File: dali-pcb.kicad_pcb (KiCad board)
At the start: 2 copper layers, 180.3 x 113 mm, 57 parts, among them J1 12-22.5V DC, J10 LOLIN-S3 (R), J11 ESP32-S3-DEVKITC-1 (L), J12 ESP32-S3-DEVKITC-1 (R), J13 LOLIN-S2-MINI (L), J14 LOLIN-S2-MINI (R), J15 DALI BUS, J16 DALI BUS, J17 FTDI-MCU, J18 A10, J19 A5-1, J2 DALI BUS, J20 A5-2, J21 A2-1, J22 A2-2, J23 A2-3, J24 A2-4, J25 A2-5, J26 D8, J27 D4-1, J28 D4-2, J29 D2-1, J3 5V DC, J30 D2-2, J31 D2-3, J32 D2-4, J33 D1-11, J34 D1-12, J35 D1-13, J36 D1-14, J37 UART-DALI, J4 5V DC, J5 5V DC, J6 5V DC, J7 5V DC, J8 GND, J9 LOLIN-S3 (L), Q1 PZT2222A, Q2 MMBT2222A, U1 TCLT1000, U2 TCLT1000

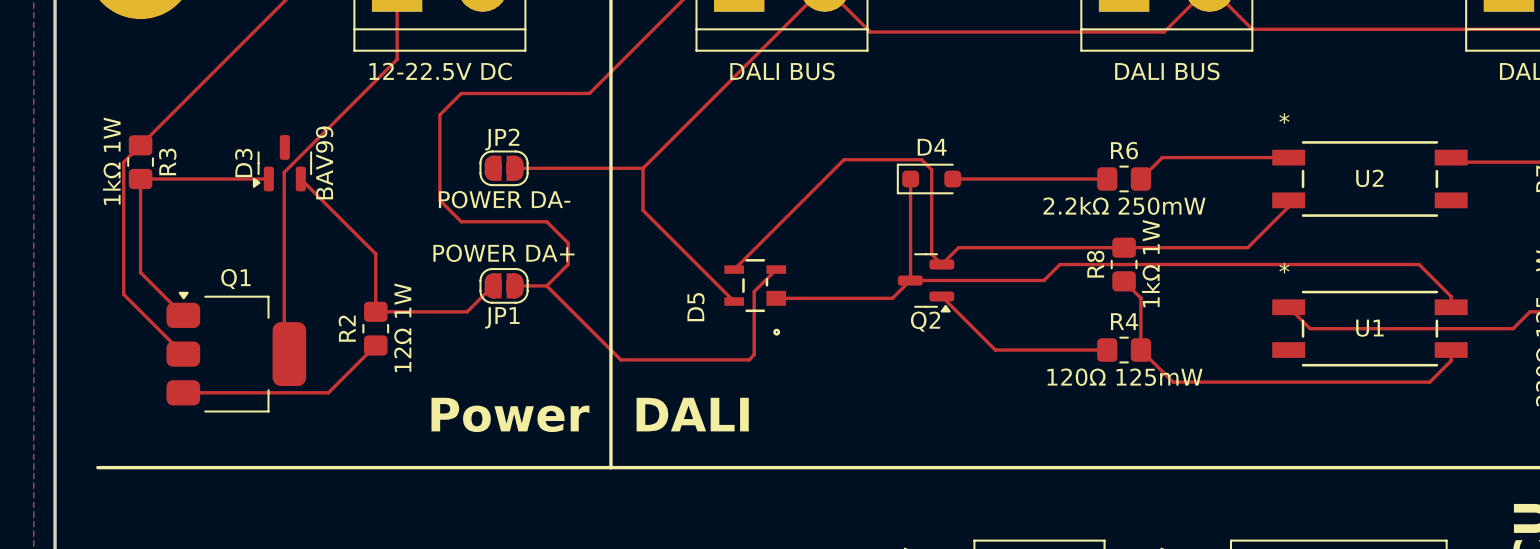
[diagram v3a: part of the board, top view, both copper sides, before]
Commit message: Rotate R3 and improve silkscreen positions
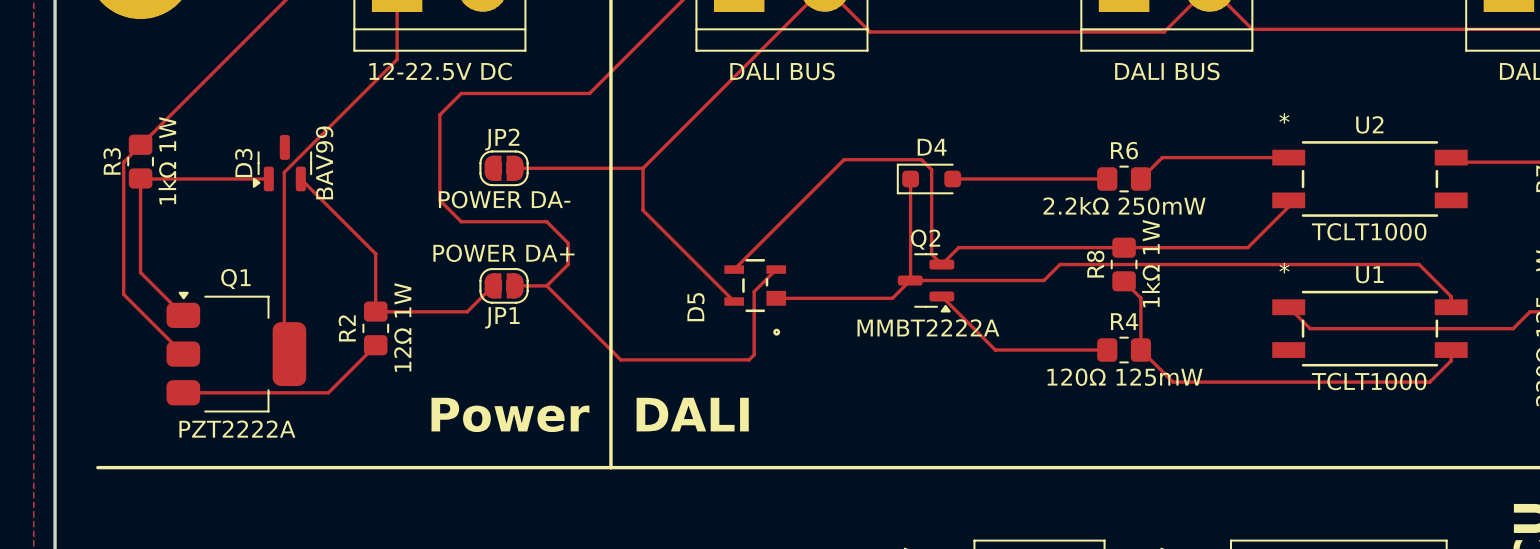
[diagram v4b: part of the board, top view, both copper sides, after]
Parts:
- turned R3 to 90 degrees
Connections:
- R3 pad 1: +12-22.5V DC -> Net-(Q1-B)
- R3 pad 2: Net-(Q1-B) -> +12-22.5V DC

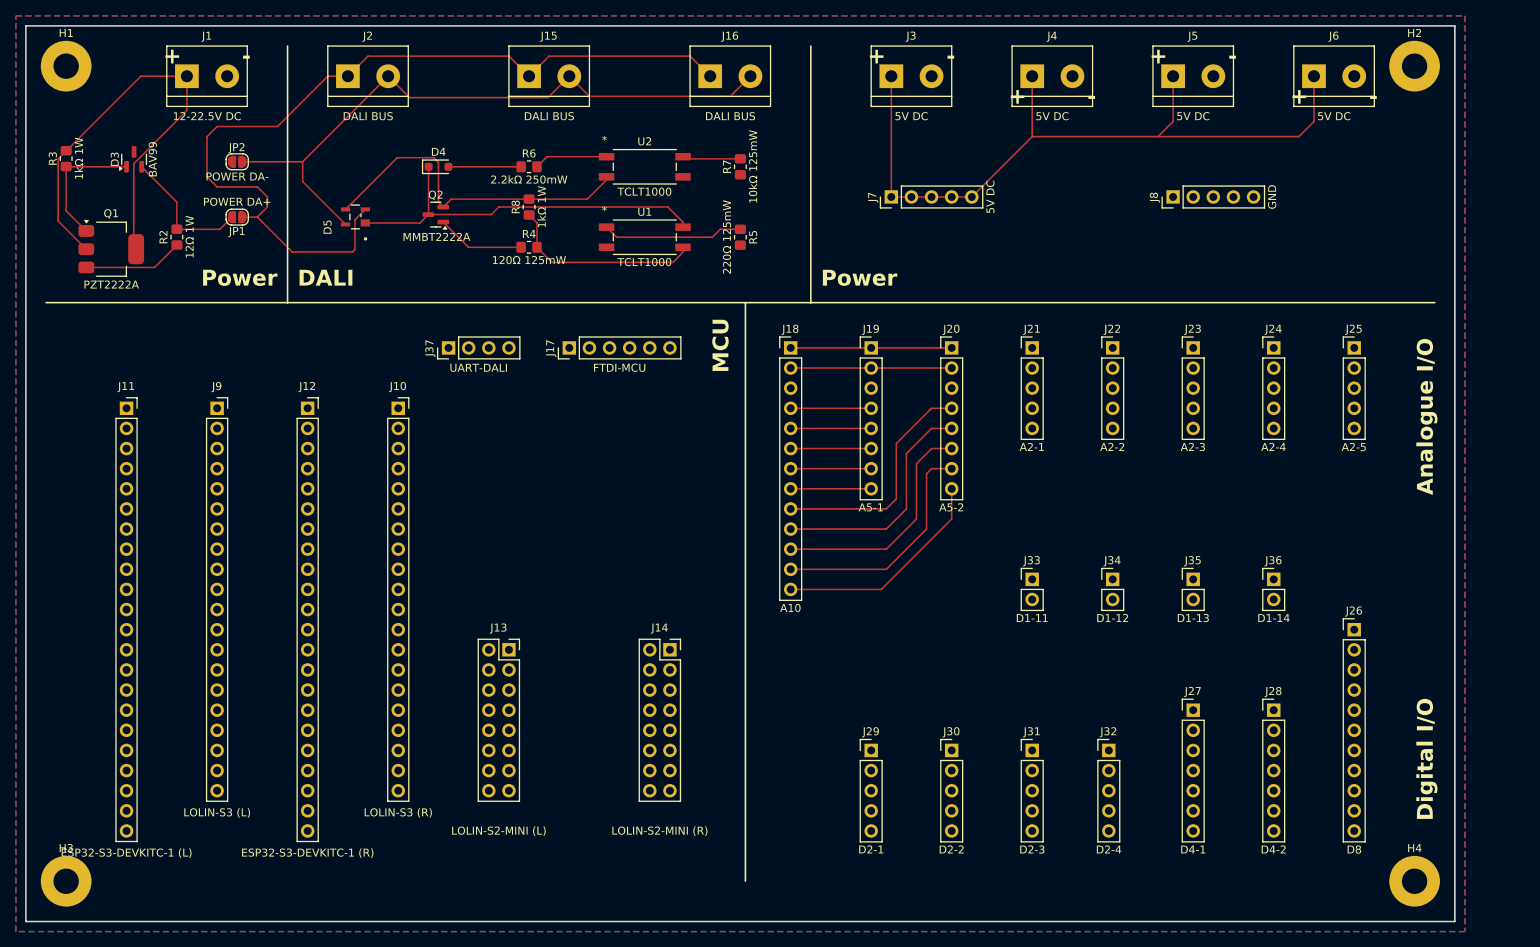
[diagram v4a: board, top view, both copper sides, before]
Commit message: Renumber references and place LOLIN-S3-MINI
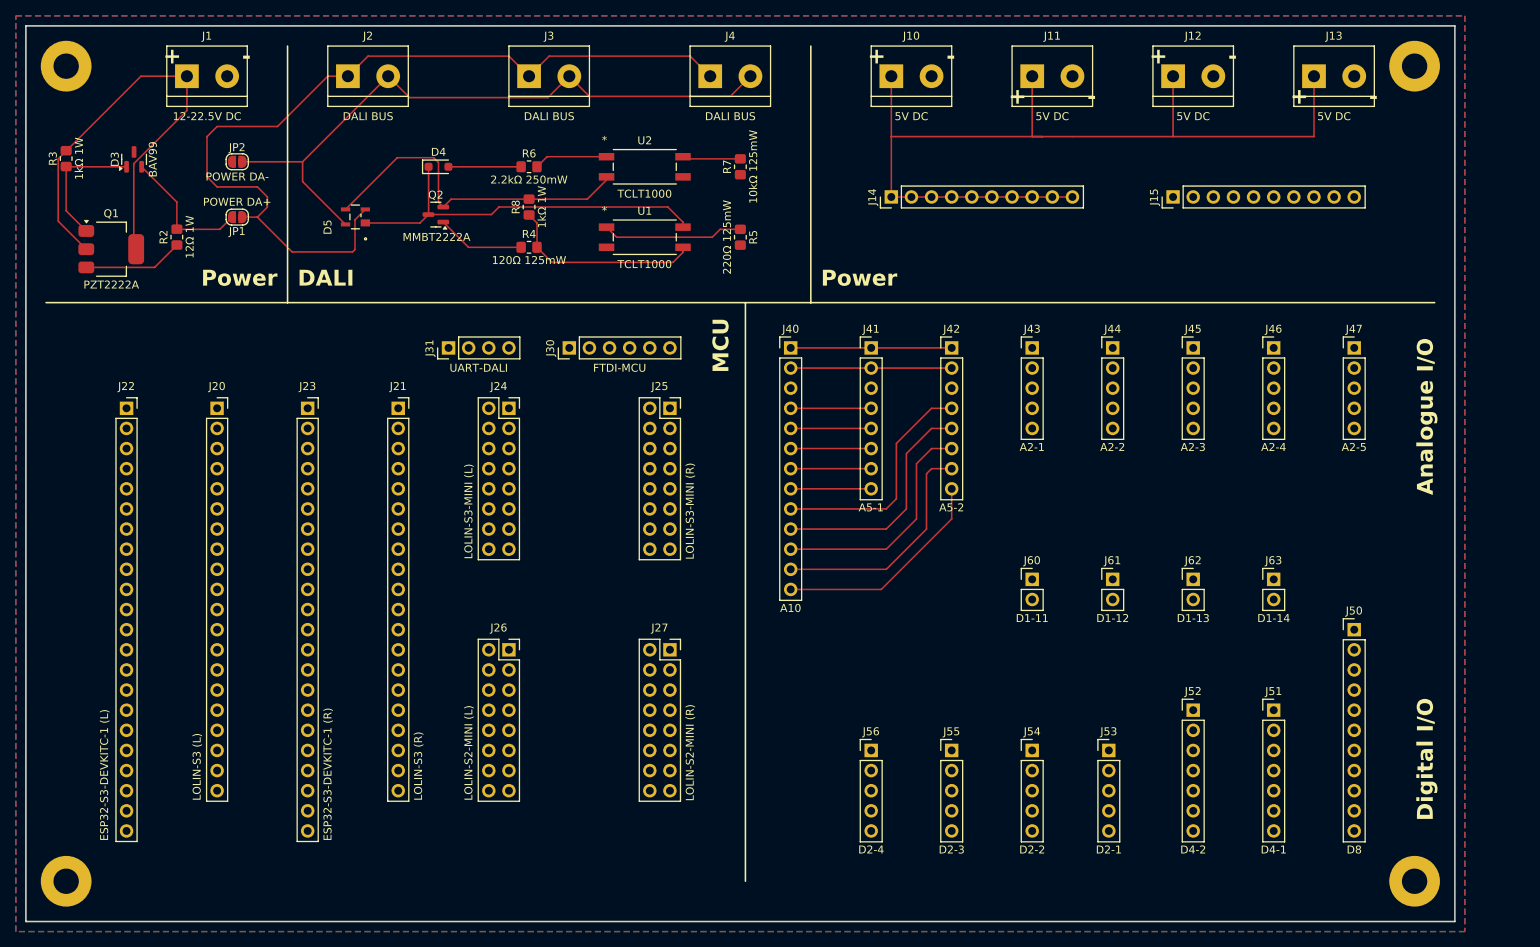
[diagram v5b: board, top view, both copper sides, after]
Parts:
- added J24: LOLIN-S3-MINI (L), Connector_PinSocket_2.54mm:PinSocket_2x08_P2.54mm_Vertical, F.Cu at (76.2, 63.5)
- added J25: LOLIN-S3-MINI (R), Connector_PinSocket_2.54mm:PinSocket_2x08_P2.54mm_Vertical, F.Cu at (96.5, 63.5)
- J14: renamed from J7; footprint Connector_PinHeader_2.54mm:PinHeader_1x05_P2.54mm_Vertical -> Connector_PinHeader_2.54mm:PinHeader_1x10_P2.54mm_Vertical
- J15: renamed from J8; footprint Connector_PinHeader_2.54mm:PinHeader_1x05_P2.54mm_Vertical -> Connector_PinHeader_2.54mm:PinHeader_1x10_P2.54mm_Vertical
- J51: renamed from J28; value D4-2 -> D4-1
- J52: renamed from J27; value D4-1 -> D4-2
- J53: renamed from J32; value D2-4 -> D2-1
- J54: renamed from J31; value D2-3 -> D2-2
- J55: renamed from J30; value D2-2 -> D2-3
- J56: renamed from J29; value D2-1 -> D2-4
- renumbered J3 to J10, J4 to J11, J5 to J12, J6 to J13, J9 to J20, J10 to J21, J11 to J22, J12 to J23, J13 to J26, J14 to J27, J15 to J3, J17 to J30, J37 to J31, J16 to J4, J18 to J40, J19 to J41, J20 to J42, J21 to J43, J22 to J44, J23 to J45, J24 to J46, J25 to J47, J26 to J50, J33 to J60, J34 to J61, J35 to J62, J36 to J63
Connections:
- J51 pad 4: /IO/IO_D16 -> /IO/IO_D11
- J51 pad 5: /IO/IO_D17 -> /IO/IO_D12
- J51 pad 6: /IO/IO_D18 -> /IO/IO_D13
- J51 pad 7: /IO/IO_D39 -> /IO/IO_D14
- J52 pad 4: /IO/IO_D11 -> /IO/IO_D16
- J52 pad 5: /IO/IO_D12 -> /IO/IO_D17
- J52 pad 6: /IO/IO_D13 -> /IO/IO_D18
- J52 pad 7: /IO/IO_D14 -> /IO/IO_D39
- J53 pad 4: /IO/IO_D18 -> /IO/IO_D11
- J53 pad 5: /IO/IO_D39 -> /IO/IO_D12
- J54 pad 4: /IO/IO_D16 -> /IO/IO_D13
- J54 pad 5: /IO/IO_D17 -> /IO/IO_D14
- J55 pad 4: /IO/IO_D13 -> /IO/IO_D16
- J55 pad 5: /IO/IO_D14 -> /IO/IO_D17
- J56 pad 4: /IO/IO_D11 -> /IO/IO_D18
- J56 pad 5: /IO/IO_D12 -> /IO/IO_D39
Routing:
- net +5V: track 114.6 -> 135.9 mm

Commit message: Add logo, URLs, version
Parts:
- added EHLAB: LOGO, LOGO, F.Cu at (112.8, 112.8)
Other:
- board text added: "V1.0.0"
- board text added: "https://edinburghhacklab.com https://github.com/edinburghhacklab/dali-pcb"
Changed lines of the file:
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@@
 		)
 	)
+	(footprint "LOGO"
+		(layer "F.Cu")
+		(at 112.776 112.776)
+		(property "Reference" "EHLAB"
+			(at 0 0 0)
+			(layer "F.SilkS")
+			(hide yes)
+			(effects
+				(font
+					(size 1.5 1.5)
+					(thickness 0.3)
+				)
+			)
+		)
+		(property "Value" "LOGO"
+			(at 0.75 0 0)
+			(layer "F.SilkS")
+			(hide yes)
+			(effects
+				(font
+					(size 1.5 1.5)
+					(thickness 0.3)
+				)
+			)
+		)
+		(property "Datasheet" ""
+			(at 0 0 0)
+			(layer "F.Fab")
+			(hide yes)
+			(effects
+				(font
+					(size 1.27 1.27)
+					(thickness 0.15)
+				)
+			)
+		)
+		(property "Description" ""
+			(at 0 0 0)
+			(layer "F.Fab")
+			(hide yes)
+			(effects
+				(font
+					(size 1.27 1.27)
+					(thickness 0.15)
+				)
+			)
+		)
+		(attr board_only exclude_from_pos_files exclude_from_bom)
+		(fp_poly
+			(pts
+				(xy 0.381 1.150055) (xy 0.381 1.919111) (xy 0 1.919111) (xy -0.381 1.919111) (xy -0.381 1.150055)
+				(xy -0.381 0.381) (xy 0 0.381) (xy 0.381 0.381)
+			)
+			(stroke
+				(width 0)
+				(type solid)
+			)
+			(fill yes)
+			(layer "F.SilkS")
+		)
+		(fp_poly
+			(pts
+				(xy 0.381 3.464278) (xy 0.381 4.233333) (xy 0 4.233333) (xy -0.381 4.233333) (xy -0.381 3.464278)
+				(xy -0.381 2.695222) (xy 0 2.695222) (xy 0.381 2.695222)
+			)
+			(stroke
+				(width 0)
+				(type solid)
+			)
+			(fill yes)
+			(layer "F.SilkS")
+		)
+		(fp_poly
+			(pts
+				(xy -1.157111 -2.30694) (xy -1.157111 -0.380547) (xy -1.541639 -0.384301) (xy -1.926167 -0.388056)
+				(xy -1.929816 -1.154132) (xy -1.933466 -1.920209) (xy -2.564816 -1.916132) (xy -2.716179 -1.915075)
+				(xy -2.841916 -1.913962) (xy -2.944623 -1.912681) (xy -3.026898 -1.91112) (xy -3.091336 -1.909169)
+				(xy -3.140535 -1.906717) (xy -3.17709 -1.90365) (xy -3.203598 -1.899859) (xy -3.222655 -1.895233)
+				(xy -3.236858 -1.889658) (xy -3.241837 -1.887097) (xy -3.324257 -1.829293) (xy -3.390494 -1.757024)
+				(xy -3.424043 -1.700492) (xy -3.456947 -1.629833) (xy -3.456947 0) (xy -3.456947 1.629833) (xy -3.424043 1.700491)
+				(xy -3.373636 1.778721) (xy -3.302067 1.847587) (xy -3.241837 1.887097) (xy -3.228865 1.893088)
+				(xy -3.212093 1.898086) (xy -3.188925 1.902203) (xy -3.156766 1.905551) (xy -3.113017 1.908239)
+				(xy -3.055084 1.910381) (xy -2.98037 1.912087) (xy -2.886278 1.913468) (xy -2.770211 1.914636) (xy -2.629574 1.915702)
+				(xy -2.564816 1.916132) (xy -1.933466 1.920208) (xy -1.929816 1.154132) (xy -1.926167 0.388055)
+				(xy -1.541639 0.384301) (xy -1.157111 0.380546) (xy -1.157111 2.30694) (xy -1.157111 4.233333) (xy -1.545167 4.233333)
+				(xy -1.933222 4.233333) (xy -1.933222 3.464278) (xy -1.933222 2.695222) (xy -2.559926 2.695222)
+				(xy -2.725689 2.695043) (xy -2.866163 2.694341) (xy -2.98428 2.692867) (xy -3.082972 2.690375) (xy -3.16517 2.686616)
+				(xy -3.233807 2.681343) (xy -3.291815 2.674307) (xy -3.342125 2.665261) (xy -3.387668 2.653957)
+				(xy -3.431378 2.640148) (xy -3.476186 2.623585) (xy -3.494919 2.616195) (xy -3.656467 2.53803) (xy -3.800366 2.438971)
+				(xy -3.89329 2.355184) (xy -4.010027 2.219179) (xy -4.104769 2.066286) (xy -4.178329 1.895187) (xy -4.179826 1.890889)
+				(xy -4.226278 1.756833) (xy -4.226278 0) (xy -4.226278 -1.756833) (xy -4.179826 -1.890889) (xy -4.106541 -2.062228)
+				(xy -4.011927 -2.2165) (xy -3.897373 -2.352217) (xy -3.76427 -2.467892) (xy -3.614007 -2.562036)
+				(xy -3.506655 -2.611436) (xy -3.458356 -2.630185) (xy -3.413091 -2.64592) (xy -3.367897 -2.658902)
+				(xy -3.319809 -2.669395) (xy -3.265862 -2.677661) (xy -3.203092 -2.683962) (xy -3.128534 -2.688561)
+				(xy -3.039224 -2.69172) (xy -2.932198 -2.693701) (xy -2.80449 -2.694766) (xy -2.653136 -2.695179)
+				(xy -2.559926 -2.695222) (xy -1.933222 -2.695222) (xy -1.933222 -3.464278) (xy -1.933222 -4.233333)
+				(xy -1.545167 -4.233333) (xy -1.157111 -4.233333)
+			)
+			(stroke
+				(width 0)
+				(type solid)
+			)
+			(fill yes)
+			(layer "F.SilkS")
+		)
+		(fp_poly
+			(pts
+				(xy 1.933222 -3.464278) (xy 1.933222 -2.695222) (xy 2.559925 -2.695222) (xy 2.723695 -2.695001)
+				(xy 2.861703 -2.694291) (xy 2.976409 -2.693027) (xy 3.07027 -2.69114) (xy 3.145744 -2.688566) (xy 3.20529 -2.685235)
+				(xy 3.251366 -2.681082) (xy 3.286429 -2.676039) (xy 3.290175 -2.67534) (xy 3.46309 -2.628274) (xy 3.623788 -2.556929)
+				(xy 3.770223 -2.463349) (xy 3.90035 -2.349581) (xy 4.012122 -2.21767) (xy 4.103494 -2.069663) (xy 4.172421 -1.907605)
+				(xy 4.213451 -1.752064) (xy 4.216789 -1.720229) (xy 4.219853 -1.662392) (xy 4.222645 -1.580772)
+				(xy 4.225163 -1.477586) (xy 4.227408 -1.355055) (xy 4.22938 -1.215396) (xy 4.231079 -1.060828) (xy 4.232505 -0.893571)
+				(xy 4.233657 -0.715842) (xy 4.234537 -0.529861) (xy 4.235143 -0.337847) (xy 4.235476 -0.142017)
+				(xy 4.235536 0.05541) (xy 4.235323 0.252214) (xy 4.234836 0.446177) (xy 4.234077 0.63508) (xy 4.233044 0.816705)
+				(xy 4.231739 0.988832) (xy 4.23016 1.149244) (xy 4.228308 1.295721) (xy 4.226182 1.426045) (xy 4.223784 1.537996)
+				(xy 4.221112 1.629357) (xy 4.218168 1.697909) (xy 4.21495 1.741432) (xy 4.213451 1.752064) (xy 4.166533 1.924258)
+				(xy 4.09533 2.084544) (xy 4.001947 2.23081) (xy 3.888493 2.360946) (xy 3.757074 2.472843) (xy 3.609798 2.56439)
+				(xy 3.448774 2.633477) (xy 3.291629 2.675132) (xy 3.257741 2.680326) (xy 3.213671 2.684616) (xy 3.156915 2.688071)
+				(xy 3.084968 2.690758) (xy 2.995326 2.692747) (xy 2.885484 2.694107) (xy 2.75294 2.694906) (xy 2.595188 2.695214)
+				(xy 2.559925 2.695222) (xy 1.933222 2.695222) (xy 1.933222 3.464278) (xy 1.933222 4.233333) (xy 1.545167 4.233333)
+				(xy 1.157111 4.233333) (xy 1.157111 2.30694) (xy 1.157111 0.380546) (xy 1.541639 0.384301) (xy 1.926167 0.388055)
+				(xy 1.929816 1.154132) (xy 1.933466 1.920208) (xy 2.564816 1.916132) (xy 2.716179 1.915075) (xy 2.841915 1.913962)
+				(xy 2.944623 1.912681) (xy 3.026898 1.91112) (xy 3.091336 1.909169) (xy 3.140534 1.906716) (xy 3.177089 1.90365)
+				(xy 3.203597 1.899859) (xy 3.222655 1.895232) (xy 3.236858 1.889658) (xy 3.241837 1.887097) (xy 3.324257 1.829292)
+				(xy 3.390494 1.757024) (xy 3.424042 1.700491) (xy 3.456946 1.629833) (xy 3.456946 0) (xy 3.456946 -1.629833)
+				(xy 3.424042 -1.700492) (xy 3.373636 -1.778721) (xy 3.302066 -1.847587) (xy 3.241837 -1.887097)
+				(xy 3.228864 -1.893088) (xy 3.212092 -1.898087) (xy 3.188925 -1.902204) (xy 3.156765 -1.905551)
+				(xy 3.113017 -1.90824) (xy 3.055084 -1.910381) (xy 2.98037 -1.912087) (xy 2.886277 -1.913468) (xy 2.770211 -1.914636)
+				(xy 2.629574 -1.915702) (xy 2.564816 -1.916132) (xy 1.933466 -1.920209) (xy 1.929816 -1.154132)
+				(xy 1.926167 -0.388056) (xy 1.541639 -0.384301) (xy 1.157111 -0.380547) (xy 1.157111 -0.768829)
+				(xy 1.157111 -1.157111) (xy 0.388055 -1.157111) (xy -0.381 -1.157111) (xy -0.381 -1.53799) (xy -0.381 -1.918868)
+				(xy 0.384528 -1.922518) (xy 1.150055 -1.926167) (xy 1.15381 -2.310695) (xy 1.157565 -2.695222) (xy 0.388282 -2.695222)
+				(xy -0.381 -2.695222) (xy -0.381 -3.083278) (xy -0.381 -3.471333) (xy 0.388055 -3.471333) (xy 1.157111 -3.471333)
+				(xy 1.157111 -3.852333) (xy 1.157111 -4.233333) (xy 1.545167 -4.233333) (xy 1.933222 -4.233333)
+			)
+			(stroke
+				(width 0)
+				(type solid)
+			)
+			(fill yes)
+			(layer "F.SilkS")
+		)
+		(embedded_fonts no)
+	)
 	(footprint "Resistor_SMD:R_0805_2012Metric_Pad1.20x1.40mm_HandSolder"
 		(placed yes)
@@
 		(fp_text user "*"
 			(at -5.08 -3.3528 0)
-			(unlocked yes)
-			(layer "F.SilkS")
-			(effects
-				(font
-					(size 1 1)
-					(thickness 0.15)
-				)
-			)
-		)
-		(fp_text user "*"
-			(at -5.08 -3.3528 0)
 			(layer "F.SilkS")
 			(effects
@@
 		(fp_text user "*"
 			(at -5.08 -3.3528 0)
-			(layer "F.SilkS")
-			(effects
-				(font
-					(size 1 1)
-					(thickness 0.15)
-				)
-			)
-		)
-		(fp_text user "*"
-			(at -5.08 -3.3528 0)
 			(unlocked yes)
 			(layer "F.SilkS")
@@
 		)
 	)
+	(gr_text "https://edinburghhacklab.com\n\nhttps://github.com/edinburghhacklab/dali-pcb"
+		(at 138.176 48.768 0)
+		(layer "F.SilkS")
+		(effects
+			(font
+				(size 1.5 1.5)
+				(thickness 0.3)
+				(bold yes)
+			)
+			(justify left bottom)
+		)
+	)
 	(gr_text "+        -"
 		(at 144.78 24.13 0)
@@
 		)
 	)
+	(gr_text "V1.0.0"
+		(at 112.776 119.888 0)
+		(layer "F.SilkS")
+		(effects
+			(font
+				(size 1.5 1.5)
+				(thickness 0.3)
+				(bold yes)
+			)
+			(justify bottom)
+		)
+	)

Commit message: Render PCB
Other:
- board size 180.3 x 113 mm -> 180.4 x 113 mm
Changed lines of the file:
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@@
 	(gr_rect
 		(start 15.24 15.24)
-		(end 195.58 128.27)
+		(end 195.64 128.24)
 		(stroke
 			(width 0.2)
